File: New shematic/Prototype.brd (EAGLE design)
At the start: 120.8 x 77.9 mm, 15 parts, among them SW1 1-1825910-4, U1 BOB-12009, U3 NUCLEO-L432KC, U4 24AA64T-I/OT

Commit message: remaked the pcb board
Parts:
- removed JP2, JP3: (no value), pinhead:1X01
- added SV2: (no value), con-lstb:MA04-1
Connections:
- removed net N$9: JP2.1, U1.LV, U3.CN4_1
- new net N$18: SV2.1, SV2.2, U1.LV, U3.CN4_1
- net GND: now also SV2.3, SV2.4; no longer JP3.1
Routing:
- net N$18: track 0.00 -> 223.9 mm, vias 0 -> 2
- net N$9: track 214.0 -> 0.00 mm, vias 2 -> 0
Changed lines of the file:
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@@
 <attribute name="VALUE" x="88.29" y="61.6" size="1.016" layer="27" rot="R180"/>
-</element>
-<element name="JP2" library="pinhead" library_urn="urn:adsk.eagle:library:325" package="1X01" package3d_urn="urn:adsk.eagle:package:22485/2" value="" x="87.58" y="34.47" smashed="yes">
-<attribute name="NAME" x="86.2338" y="36.2988" size="1.27" layer="25" ratio="10"/>
-<attribute name="VALUE" x="86.31" y="31.295" size="1.27" layer="27"/>
-</element>
-<element name="JP3" library="pinhead" library_urn="urn:adsk.eagle:library:325" package="1X01" package3d_urn="urn:adsk.eagle:package:22485/2" value="" x="94.77" y="34.79" smashed="yes">
-<attribute name="NAME" x="93.4238" y="36.6188" size="1.27" layer="25" ratio="10"/>
-<attribute name="VALUE" x="93.5" y="31.615" size="1.27" layer="27"/>
 </element>
 <element name="R1" library="rcl" library_urn="urn:adsk.eagle:library:334" package="R1206W" package3d_urn="urn:adsk.eagle:package:23539/2" value="2k2" x="83.9" y="40.05" smashed="yes" rot="R180">
@@
 <attribute name="PRICE" value="None" x="17.77" y="62.69" size="1.778" layer="27" rot="R180" display="off"/>
 <attribute name="VALUE" x="24.27" y="71.19" size="1.27" layer="27" rot="R180" align="top-left"/>
+</element>
+<element name="SV2" library="con-lstb" library_urn="urn:adsk.eagle:library:162" package="MA04-1" package3d_urn="urn:adsk.eagle:package:8337/1" value="" x="117.84" y="15.28" smashed="yes" rot="R90">
+<attribute name="MF" value="" x="117.84" y="15.28" size="1.778" layer="27" rot="R90" display="off"/>
+<attribute name="MPN" value="" x="117.84" y="15.28" size="1.778" layer="27" rot="R90" display="off"/>
+<attribute name="NAME" x="116.189" y="10.2" size="1.27" layer="25" ratio="10" rot="R90"/>
+<attribute name="OC_FARNELL" value="unknown" x="117.84" y="15.28" size="1.778" layer="27" rot="R90" display="off"/>
+<attribute name="OC_NEWARK" value="unknown" x="117.84" y="15.28" size="1.778" layer="27" rot="R90" display="off"/>
+<attribute name="VALUE" x="116.189" y="15.915" size="1.27" layer="27" ratio="10" rot="R90"/>
 </element>
 </elements>
@@
 <contactref element="U1" pad="GND_1"/>
 <contactref element="U1" pad="GND_2"/>
-<contactref element="JP3" pad="1"/>
+<contactref element="SV2" pad="4"/>
+<contactref element="SV2" pad="3"/>
 <wire x1="86.615" y1="59.95" x2="79.16" y2="60.34" width="0" layer="19" extent="1-1"/>
 <wire x1="73.79" y1="43.855" x2="79.16" y2="60.34" width="0" layer="19" extent="1-1"/>
@@
 <wire x1="29.21" y1="26.67" x2="29.21" y2="10.16" width="0.8128" layer="1"/>
 <wire x1="29.21" y1="10.16" x2="36.83" y2="2.54" width="0.8128" layer="1"/>
-<wire x1="36.83" y1="2.54" x2="80.01" y2="2.54" width="0.8128" layer="1"/>
+<wire x1="80.01" y1="2.54" x2="36.83" y2="2.54" width="0.8128" layer="1"/>
 <wire x1="80.01" y1="2.54" x2="82.55" y2="5.08" width="0.8128" layer="1"/>
 <wire x1="82.55" y1="5.08" x2="82.55" y2="15.24" width="0.8128" layer="1"/>
 <wire x1="82.55" y1="15.24" x2="81.28" y2="16.51" width="0.8128" layer="1"/>
-<wire x1="81.28" y1="16.51" x2="72.39" y2="16.51" width="0.8128" layer="1"/>
+<wire x1="81.28" y1="16.51" x2="80.01" y2="16.51" width="0.8128" layer="1"/>
 <via x="72.39" y="16.51" extent="1-16" drill="0.35"/>
+<wire x1="80.01" y1="16.51" x2="72.39" y2="16.51" width="0.8128" layer="1"/>
 <wire x1="72.39" y1="16.51" x2="68.58" y2="16.51" width="0.8128" layer="16"/>
 <via x="68.58" y="16.51" extent="1-16" drill="0.35"/>
@@
 <wire x1="16.51" y1="34.29" x2="16.51" y2="29.21" width="0.8128" layer="1"/>
 </signal>
-<signal name="N$9">
+<signal name="N$10">
+<contactref element="SDS011" pad="2"/>
+<contactref element="U1" pad="HV"/>
+<wire x1="10.15" y1="32.45" x2="6.35" y2="36.25" width="0.8128" layer="1"/>
+<wire x1="6.35" y1="55.08" x2="12.69" y2="61.42" width="0.8128" layer="1"/>
+<wire x1="6.35" y1="36.25" x2="6.35" y2="55.08" width="0.8128" layer="1"/>
+</signal>
+<signal name="N$11">
+<via x="15.4289625" y="9.9990625" extent="1-16" drill="5.5"/>
+</signal>
+<signal name="N$12">
+<via x="105.5" y="10" extent="1-16" drill="5.5"/>
+</signal>
+<signal name="N$13">
+<via x="105.5" y="47.5" extent="1-16" drill="5.5"/>
+</signal>
+<signal name="N$16">
+<via x="15.5" y="47.5" extent="1-16" drill="5.5"/>
+</signal>
+<signal name="N$7">
+<via x="25" y="29" extent="1-16" drill="5"/>
+</signal>
+<signal name="N$8">
+<via x="75" y="29" extent="1-16" drill="5"/>
+</signal>
+<signal name="N$18">
+<contactref element="SV2" pad="1"/>
+<contactref element="SV2" pad="2"/>
 <contactref element="U1" pad="LV"/>
 <contactref element="U3" pad="CN4_1"/>
-<contactref element="JP2" pad="1"/>
-<wire x1="87.58" y1="34.47" x2="86.88" y2="33.77" width="0.8128" layer="1"/>
-<wire x1="86.88" y1="33.77" x2="85.09" y2="31.98" width="0.8128" layer="1"/>
-<wire x1="85.09" y1="31.98" x2="85.09" y2="27.94" width="0.8128" layer="1"/>
 <wire x1="57.545" y1="45.325" x2="51.2" y2="45.325" width="0.8128" layer="1"/>
 <wire x1="62.23" y1="40.64" x2="57.545" y2="45.325" width="0.8128" layer="1"/>
-<wire x1="86.88" y1="33.77" x2="89.65" y2="33.77" width="0.8128" layer="1"/>
-<wire x1="89.65" y1="33.77" x2="93.98" y2="38.1" width="0.8128" layer="1"/>
-<wire x1="93.98" y1="38.1" x2="96.52" y2="38.1" width="0.8128" layer="1"/>
-<wire x1="96.52" y1="38.1" x2="99.06" y2="35.56" width="0.8128" layer="1"/>
-<wire x1="99.06" y1="35.56" x2="99.06" y2="33.02" width="0.8128" layer="1"/>
 <wire x1="29.67" y1="61.42" x2="22.85" y2="61.42" width="0.8128" layer="1"/>
-<wire x1="104.14" y1="27.94" x2="107.95" y2="27.94" width="0.8128" layer="1"/>
-<wire x1="99.06" y1="33.02" x2="104.14" y2="27.94" width="0.8128" layer="1"/>
 <wire x1="113.03" y1="33.02" x2="113.03" y2="52.07" width="0.8128" layer="1"/>
 <wire x1="107.95" y1="27.94" x2="113.03" y2="33.02" width="0.8128" layer="1"/>
@@
 <via x="62.23" y="30.48" extent="1-16" drill="0.35"/>
 <wire x1="62.23" y1="30.48" x2="62.23" y2="40.64" width="0.8128" layer="1"/>
-<wire x1="80.01" y1="22.86" x2="73.66" y2="22.86" width="0.8128" layer="1"/>
+<wire x1="73.66" y1="22.86" x2="80.01" y2="22.86" width="0.8128" layer="1"/>
 <via x="73.66" y="22.86" extent="1-16" drill="0.35"/>
 <wire x1="73.66" y1="22.86" x2="69.85" y2="22.86" width="0.8128" layer="16"/>
 <wire x1="69.85" y1="22.86" x2="62.23" y2="30.48" width="0.8128" layer="16"/>
-<wire x1="85.09" y1="27.94" x2="80.01" y2="22.86" width="0.8128" layer="1"/>
-</signal>
-<signal name="N$10">
-<contactref element="SDS011" pad="2"/>
-<contactref element="U1" pad="HV"/>
-<wire x1="10.15" y1="32.45" x2="6.35" y2="36.25" width="0.8128" layer="1"/>
-<wire x1="6.35" y1="55.08" x2="12.69" y2="61.42" width="0.8128" layer="1"/>
-<wire x1="6.35" y1="36.25" x2="6.35" y2="55.08" width="0.8128" layer="1"/>
-</signal>
-<signal name="N$11">
-<via x="15.4289625" y="9.9990625" extent="1-16" drill="5.5"/>
-</signal>
-<signal name="N$12">
-<via x="105.5" y="10" extent="1-16" drill="5.5"/>
-</signal>
-<signal name="N$13">
-<via x="105.5" y="47.5" extent="1-16" drill="5.5"/>
-</signal>
-<signal name="N$16">
-<via x="15.5" y="47.5" extent="1-16" drill="5.5"/>
-</signal>
-<signal name="N$7">
-<via x="25" y="29" extent="1-16" drill="5"/>
-</signal>
-<signal name="N$8">
-<via x="75" y="29" extent="1-16" drill="5"/>
+<wire x1="117.84" y1="11.47" x2="117.84" y2="14.01" width="0.8128" layer="1"/>
+<wire x1="80.01" y1="22.86" x2="85.09" y2="27.94" width="0.8128" layer="1"/>
+<wire x1="85.09" y1="27.94" x2="107.95" y2="27.94" width="0.8128" layer="1"/>
+<wire x1="117.84" y1="11.47" x2="107.95" y2="21.36" width="0.8128" layer="1"/>
+<wire x1="107.95" y1="21.36" x2="107.95" y2="27.94" width="0.8128" layer="1"/>
 </signal>
 </signals>
@@
 <mfgpreviewcolor name="substratecolor" color="0xFF786E46"/>
 </mfgpreviewcolors>
+<errors>
+</errors>
 </board>
 </drawing>

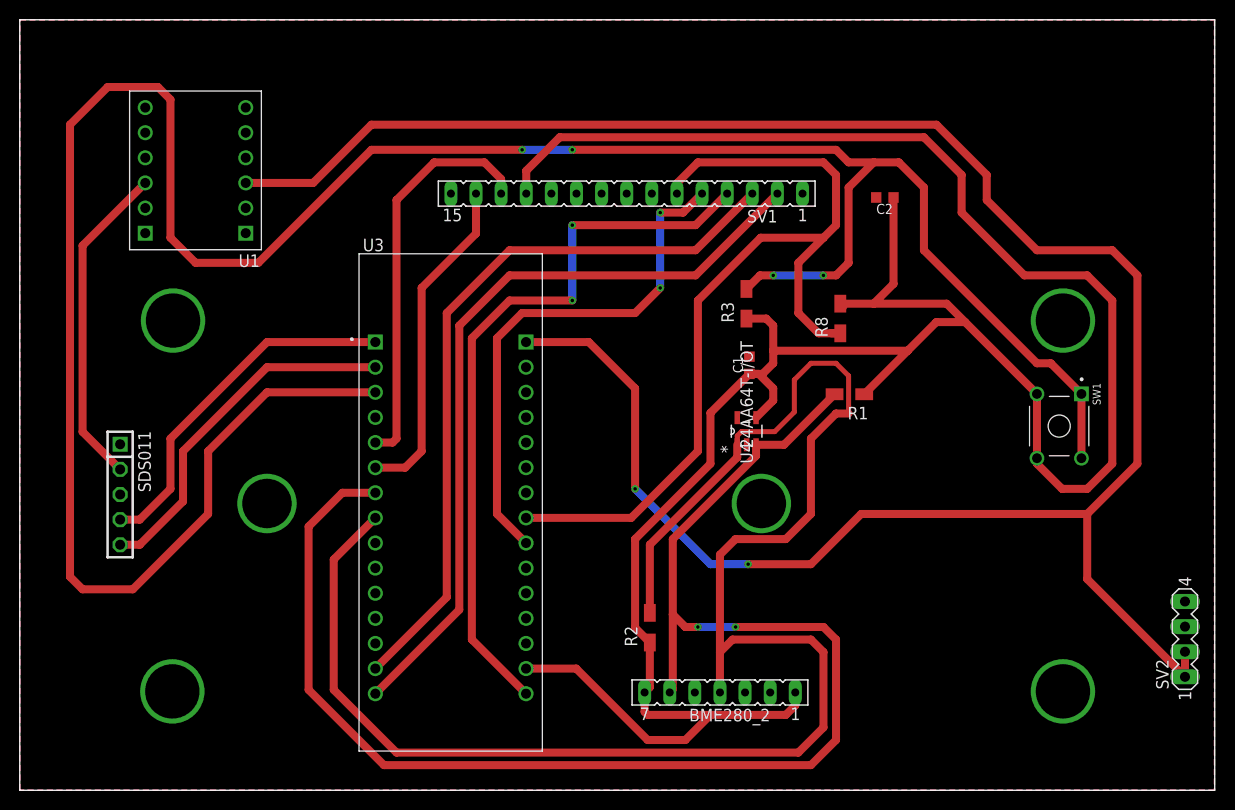
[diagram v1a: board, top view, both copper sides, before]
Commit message: refactored the shematic and added components so that sensor can go in sleep
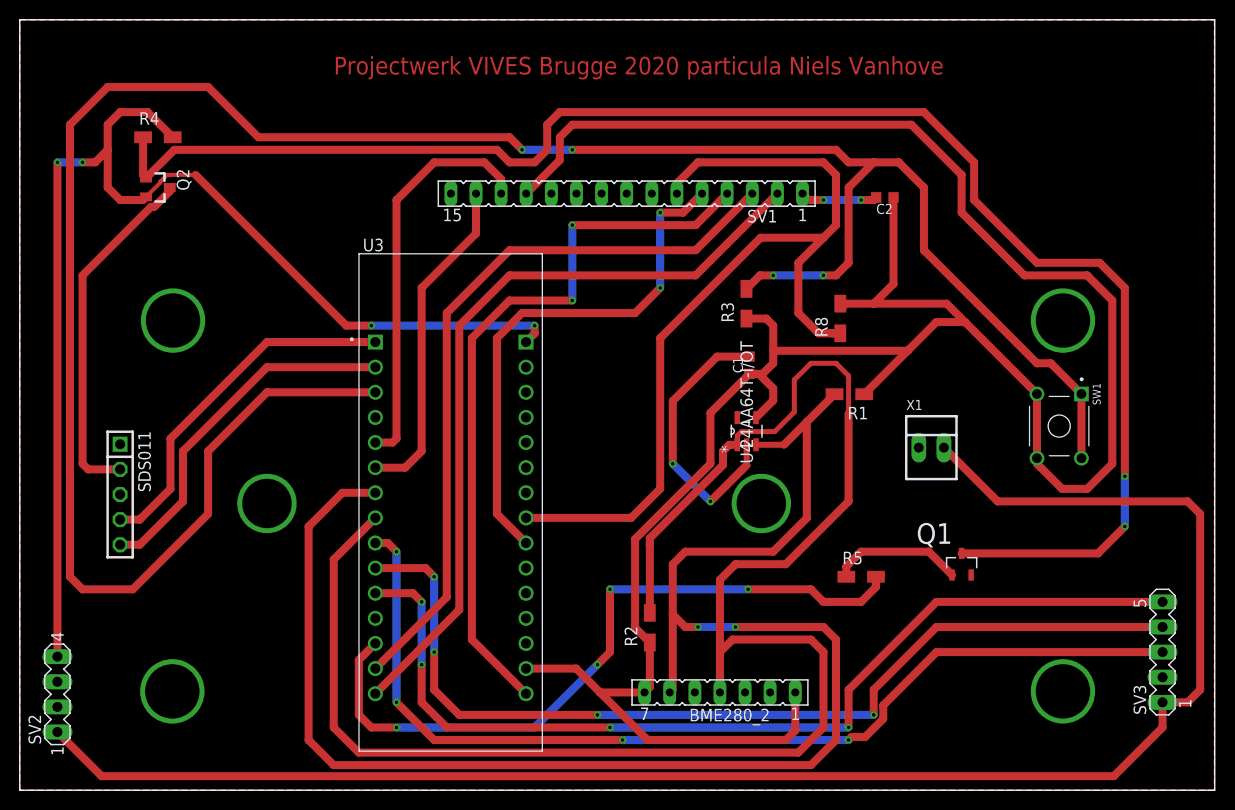
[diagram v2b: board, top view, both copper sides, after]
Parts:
- removed U1: BOB-12009, BOB-12009:CONV_BOB-12009
- added Q1: MMBT4401, LM3480IM3-5.0:SOT95P263X110-3N
- added Q2: NTR410PT1G, BSS84LT1:SOT23
- added R4: 100k, rcl:R1206W
- added R5: 1M, rcl:R1206W
- added SV3: (no value), con-lstb:MA05-1
- added X1: 22-23-2021, con-molex:22-23-2021
- moved SV2 114.2 mm to (3.81, 9.70)
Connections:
- new net N$21: Q1.1, R5.1
- new net N$22: SV2.1, SV3.1, X1.2
- new net N$24: SV3.3, U3.CN3_9
- new net N$25: SV3.4, U3.CN3_10
- new net N$26: SV3.5, U3.CN3_11
- new net N$29: R5.2, U3.CN3_13
- new net N$9: Q1.3, Q2.1, R4.1
- net GND: now also Q1.2, SV2.2, SV3.2, X1.1; no longer SV2.4, U1.GND_1, U1.GND_2
- net N$10: now also Q2.3; no longer U1.HV
- net N$18: now also Q2.2, R4.2, SV2.4; no longer SV2.1, SV2.2, U1.LV
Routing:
- net N$22: track 0.00 -> 169.0 mm
- net N$9: track 0.00 -> 159.9 mm, vias 0 -> 2
- net N$24: track 0.00 -> 101.3 mm, vias 0 -> 4
- net N$18: track 223.9 -> 123.3 mm, vias 2 -> 4
- net N$26: track 0.00 -> 98.7 mm, vias 0 -> 4
- net N$25: track 0.00 -> 97.6 mm, vias 0 -> 4
- net N$29: track 0.00 -> 72.4 mm, vias 0 -> 4
- net GND: track 0.00 -> 36.4 mm, vias 0 -> 4
- net N$5: track 256.3 -> 238.7 mm
- net N$21: track 0.00 -> 13.3 mm
- net N$23: track 148.7 -> 161.3 mm
- net N$10: track 33.2 -> 35.8 mm
- net N$4: track 170.9 -> 172.9 mm
- net VCC: track 263.7 -> 262.0 mm
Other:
- board text added: "Projectwerk VIVES Brugge 2020 particula Niels Vanhove"
